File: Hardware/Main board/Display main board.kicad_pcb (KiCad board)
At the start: 2 copper layers, 142.2 x 91.4 mm, 55 parts, among them J1 Board to Board, J3 Conn_01x03, P1 USB_C_Plug_USB2.0, U1 BQ25895RTW, U10 W25Q32JVSS, U2 ABM8-272-T3, U4 RP2040, U5 AP7361C-33E, U6 AP7361C-33E, U7 AP7361C-33E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

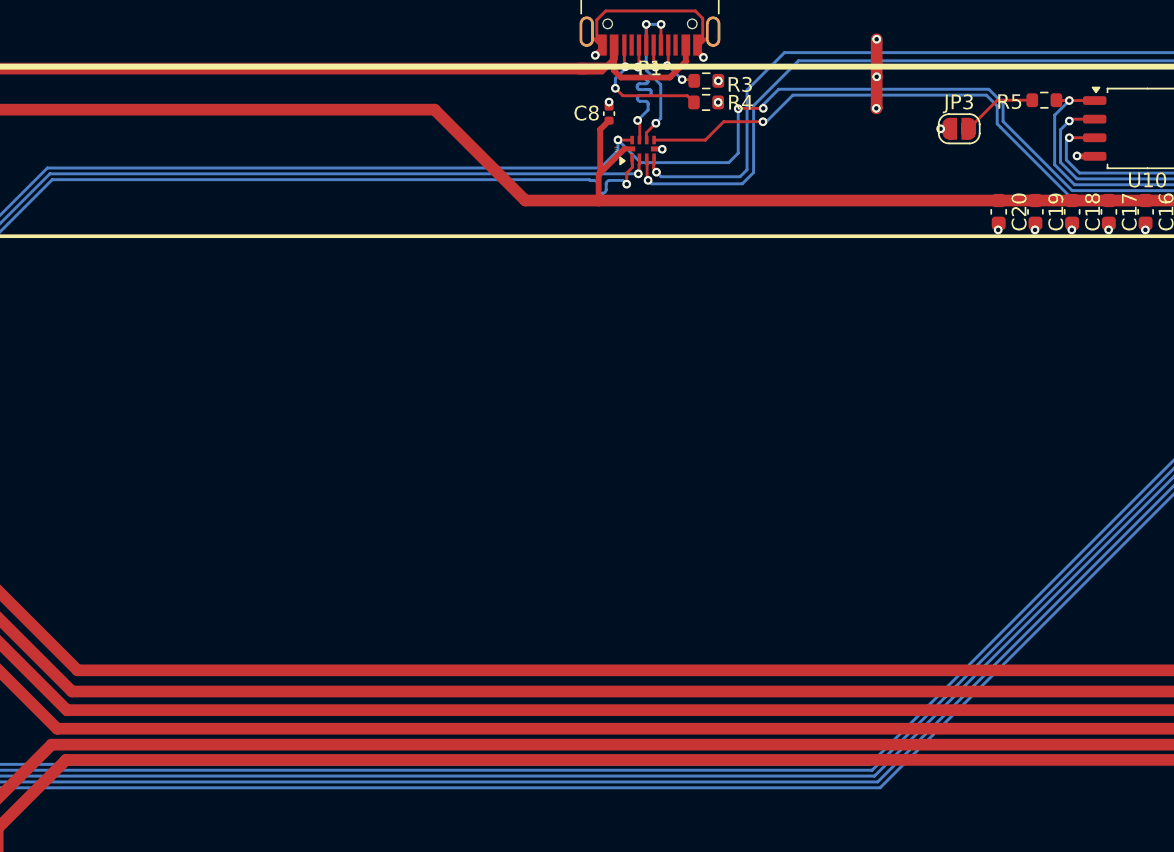
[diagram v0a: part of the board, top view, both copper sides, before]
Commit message: add battery label
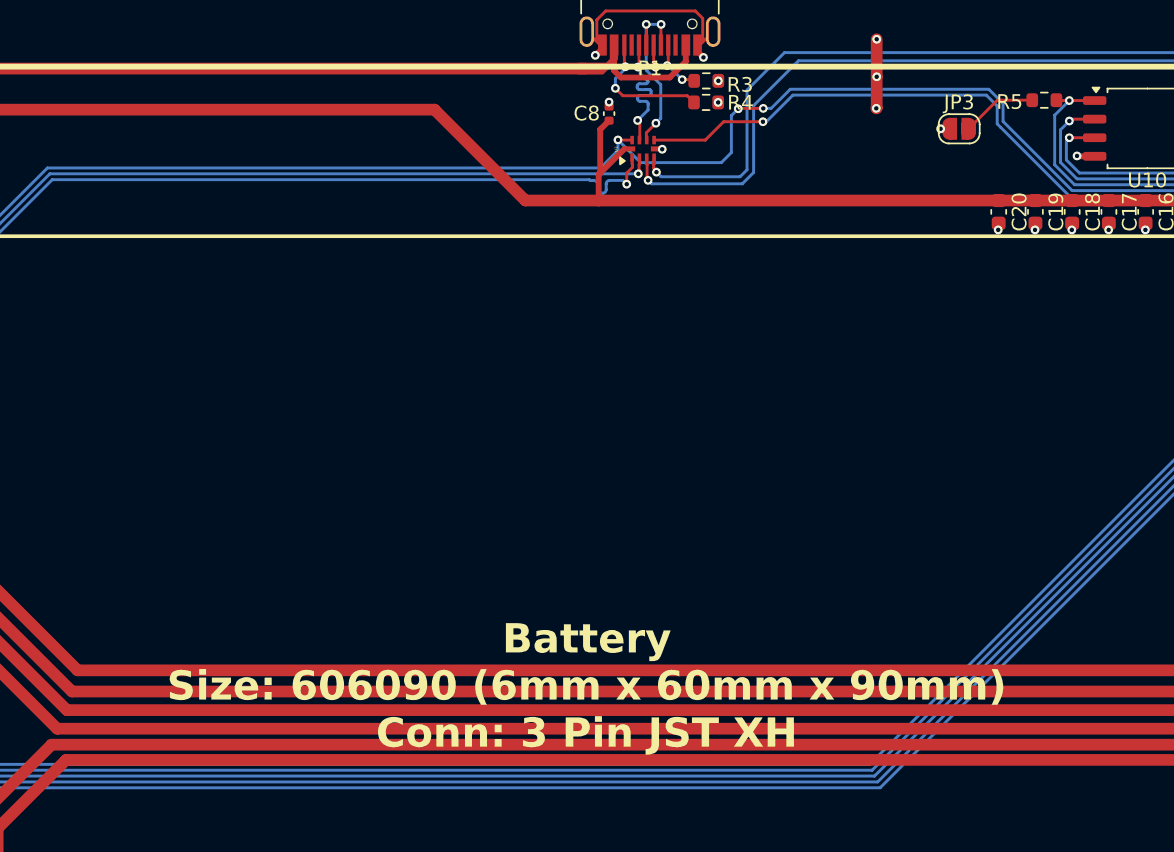
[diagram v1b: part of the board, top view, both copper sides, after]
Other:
- board text added: "Battery Size: 606090 (6mm x 60mm x 90mm) Conn: 3 Pin JST XH"
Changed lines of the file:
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@@
 		)
 	)
+	(gr_text "Battery\nSize: 606090 (6mm x 60mm x 90mm)\nConn: 3 Pin JST XH"
+		(at 132.842 107.1372 0)
+		(layer "F.SilkS")
+		(effects
+			(font
+				(size 2 2)
+				(thickness 0.4)
+				(bold yes)
+			)
+			(justify bottom)
+		)
+	)
 	(gr_text "+3V3-1\n+3V3-3\n+5V\nMB_SDA\nGND"
 		(at 193.569237 101.6 90)
@@
 	)
 	(segment
-		(start 179.658256 68.891)
-		(end 182.261 71.493744)
+		(start 133.771871 67.345329)
+		(end 134.9756 66.1416)
 		(width 0.2)
 		(layer "B.Cu")
@@
 	)
 	(segment
-		(start 182.261 71.493744)
-		(end 182.261 71.938475)
+		(start 85.766808 106.9024)
+		(end 88.83 106.9024)
 		(width 0.2)
 		(layer "B.Cu")
@@
 	)
 	(segment
-		(start 133.771871 67.345329)
-		(end 134.9756 66.1416)
+		(start 144.903032 63.273697)
+		(end 145.438103 63.273697)
 		(width 0.2)
 		(layer "B.Cu")
@@
 	)
 	(segment
-		(start 136.525 66.9798)
-		(end 134.9756 65.4304)
+		(start 89.545 106.1874)
+		(end 89.545 73.782114)
 		(width 0.2)
 		(layer "B.Cu")
@@
 	)
 	(segment
-		(start 183.880925 73.5584)
-		(end 190.614397 73.5584)
+		(start 145.438103 63.273697)
+		(end 146.7458 61.966)
 		(width 0.2)
 		(layer "B.Cu")
@@
 	)
 	(segment
-		(start 85.766808 106.9024)
-		(end 88.83 106.9024)
+		(start 85.566808 106.7024)
+		(end 85.766808 106.9024)
 		(width 0.2)
 		(layer "B.Cu")
@@
 	)
 	(segment
-		(start 89.545 106.1874)
-		(end 89.545 73.782114)
+		(start 166.013628 68.891)
+		(end 179.658256 68.891)
 		(width 0.2)
 		(layer "B.Cu")
@@
 	)
 	(segment
-		(start 85.566808 106.7024)
-		(end 85.766808 106.9024)
+		(start 179.658256 68.891)
+		(end 182.261 71.493744)
 		(width 0.2)
 		(layer "B.Cu")
@@
 	)
 	(segment
-		(start 160.3148 61.966)
-		(end 161.29 62.9412)
+		(start 146.7458 61.966)
+		(end 160.3148 61.966)
 		(width 0.2)
 		(layer "B.Cu")
@@
 	)
 	(segment
-		(start 143.193 66.3316)
-		(end 142.5448 66.9798)
+		(start 136.525 66.9798)
+		(end 134.9756 65.4304)
 		(width 0.2)
 		(layer "B.Cu")
@@
 	)
 	(segment
-		(start 143.193 63.2968)
-		(end 143.193 66.3316)
+		(start 183.880925 73.5584)
+		(end 190.614397 73.5584)
 		(width 0.2)
 		(layer "B.Cu")
@@
 	)
 	(segment
-		(start 144.903032 63.021368)
-		(end 145.9584 61.966)
+		(start 142.0368 66.9798)
+		(end 136.525 66.9798)
 		(width 0.2)
 		(layer "B.Cu")
@@
 	)
 	(segment
-		(start 190.614397 73.5584)
-		(end 190.846928 73.325869)
+		(start 182.261 71.938475)
+		(end 183.880925 73.5584)
+		(width 0.2)
+		(layer "B.Cu")
+		(net 21)
+	)
+	(segment
+		(start 142.7226 63.7672)
+		(end 142.7226 66.294)
 		(width 0.2)
 		(layer "B.Cu")
@@
 	)
 	(segment
-		(start 145.9584 61.966)
-		(end 160.3148 61.966)
+		(start 143.193 63.2968)
+		(end 142.7226 63.7672)
 		(width 0.2)
 		(layer "B.Cu")
@@
 	)
 	(segment
-		(start 161.29 62.9412)
-		(end 161.29 64.167372)
+		(start 182.261 71.493744)
+		(end 182.261 71.938475)
 		(width 0.2)
 		(layer "B.Cu")
@@
 	)
 	(segment
-		(start 142.5448 66.9798)
-		(end 136.525 66.9798)
+		(start 161.29 64.167372)
+		(end 166.013628 68.891)
 		(width 0.2)
 		(layer "B.Cu")
@@
 	)
 	(segment
-		(start 134.9756 66.1416)
-		(end 134.9756 65.4304)
+		(start 190.614397 73.5584)
+		(end 190.846928 73.325869)
 		(width 0.2)
 		(layer "B.Cu")
@@
 	)
 	(segment
-		(start 182.261 71.938475)
-		(end 183.880925 73.5584)
+		(start 134.9756 66.1416)
+		(end 134.9756 65.4304)
 		(width 0.2)
 		(layer "B.Cu")
@@
 	)
 	(segment
-		(start 161.29 64.167372)
-		(end 166.013628 68.891)
+		(start 160.3148 61.966)
+		(end 161.29 62.9412)
 		(width 0.2)
 		(layer "B.Cu")
@@
 	)
 	(segment
-		(start 166.013628 68.891)
-		(end 179.658256 68.891)
+		(start 142.7226 66.294)
+		(end 142.0368 66.9798)
 		(width 0.2)
 		(layer "B.Cu")
@@
 	)
 	(segment
-		(start 144.903032 63.273697)
-		(end 144.903032 63.021368)
+		(start 161.29 62.9412)
+		(end 161.29 64.167372)
 		(width 0.2)
 		(layer "B.Cu")

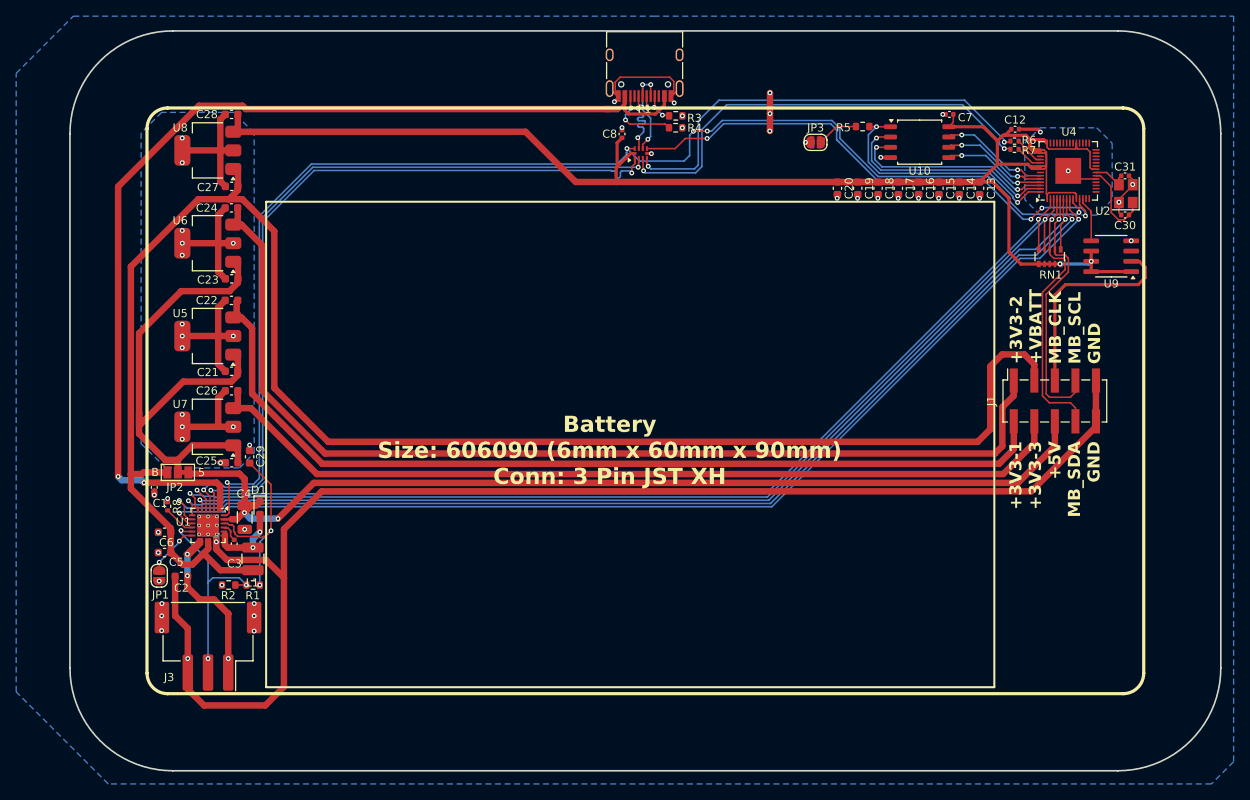
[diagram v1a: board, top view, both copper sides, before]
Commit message: Link USB-C port 3d model
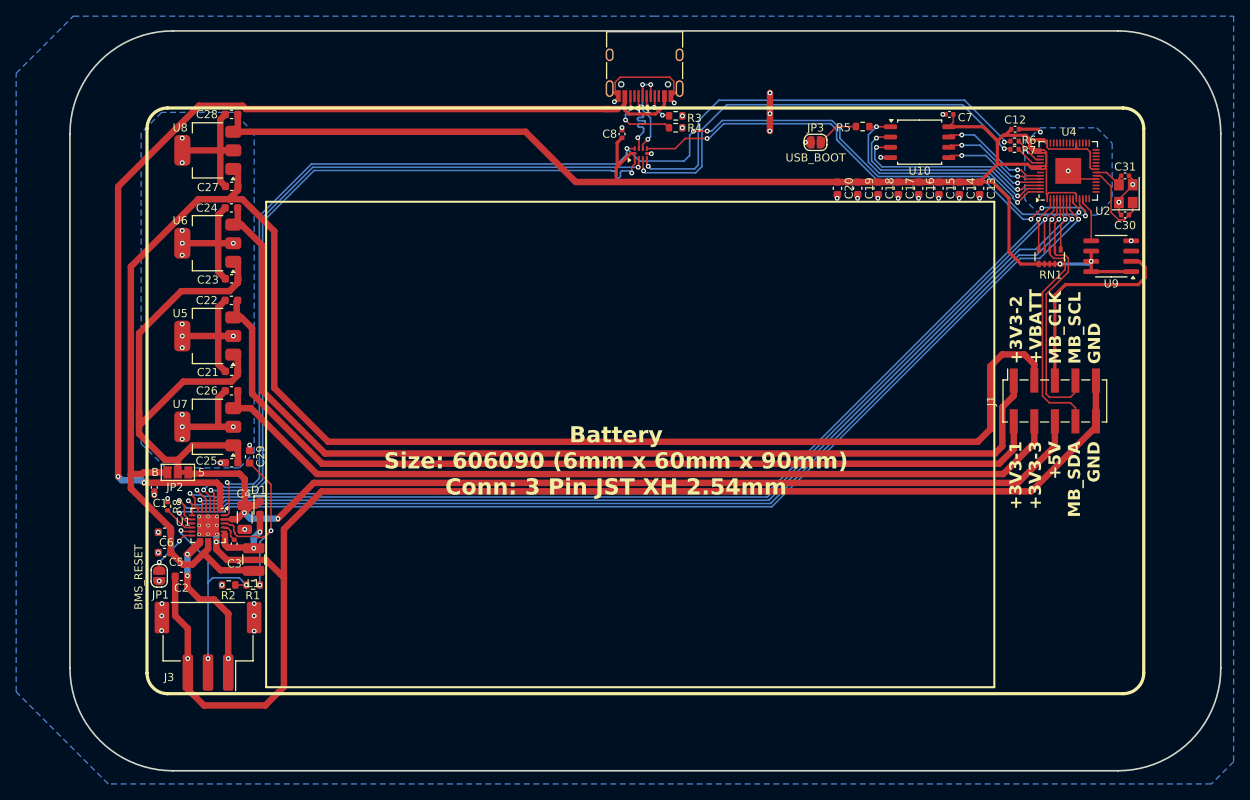
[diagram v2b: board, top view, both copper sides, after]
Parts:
- moved L1 0.13 mm to (88.8, 116.2)
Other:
- board text added: "Battery Size: 606090 (6mm x 60mm x 90mm) Conn: 3 Pin JST XH 2.54mm"
- board text removed: "Battery Size: 606090 (6mm x 60mm x 90mm) Conn: 3 Pin JST XH"
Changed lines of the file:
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@@
 		(property "Value" "USB_BOOT"
 			(at 0 1.9 0)
-			(layer "F.Fab")
+			(layer "F.SilkS")
 			(effects
 				(font
@@
 	(footprint "Inductor_SMD:L_1210_3225Metric"
 		(layer "F.Cu")
-		(at 88.7476 116.151201 -90)
+		(at 88.8492 116.2304 -90)
 		(descr "Inductor SMD 1210 (3225 Metric), square (rectangular) end terminal, IPC_7351 nominal, (Body size source: http://www.tortai-tech.com/upload/download/2011102023233369053.pdf), generated with kicad-footprint-generator")
 		(tags "inductor")
@@
 		)
 		(property "Value" "BMS_RESET"
-			(at -1.5136 -2.5908 90)
-			(layer "F.Fab")
+			(at -0.1778 -2.54 90)
+			(layer "F.SilkS")
 			(effects
 				(font
@@
 			)
 		)
+		(model "${KICAD8_3DMODEL_DIR}/Connector_USB.3dshapes/USB_C_Receptacle_GCT_USB4105-xx-A_16P_TopMnt_Horizontal.wrl"
+			(offset
+				(xyz 0 0 0)
+			)
+			(scale
+				(xyz 1 1 1)
+			)
+			(rotate
+				(xyz 0 0 0)
+			)
+		)
 	)
 	(footprint "Capacitor_SMD:C_0402_1005Metric"
@@
 		)
 	)
-	(gr_text "Battery\nSize: 606090 (6mm x 60mm x 90mm)\nConn: 3 Pin JST XH"
-		(at 132.842 107.1372 0)
+	(gr_text "Battery\nSize: 606090 (6mm x 60mm x 90mm)\nConn: 3 Pin JST XH 2.54mm"
+		(at 133.6294 108.4326 0)
 		(layer "F.SilkS")
 		(effects
@@
 	)
 	(segment
+		(start 84.7344 117.5512)
+		(end 82.6516 115.4684)
+		(width 0.8)
+		(layer "F.Cu")
+		(net 9)
+	)
+	(segment
+		(start 88.8492 117.630399)
+		(end 88.770001 117.5512)
+		(width 0.8)
+		(layer "F.Cu")
+		(net 9)
+	)
+	(segment
 		(start 78.6006 115.3668)
 		(end 78.6006 112.8568)
@@
 	)
 	(segment
-		(start 84.7344 117.5512)
-		(end 82.6516 115.4684)
-		(width 0.8)
-		(layer "F.Cu")
-		(net 9)
-	)
-	(segment
 		(start 91.3892 75.64424)
 		(end 91.3892 95.0214)
@@
 	)
 	(segment
-		(start 88.7476 117.5512)
-		(end 84.7344 117.5512)
-		(width 0.8)
-		(layer "F.Cu")
-		(net 9)
-	)
-	(segment
 		(start 179.8828 100.1268)
 		(end 179.8828 92.3544)
@@
 	)
 	(segment
+		(start 88.770001 117.5512)
+		(end 84.7344 117.5512)
+		(width 0.8)
+		(layer "F.Cu")
+		(net 9)
+	)
+	(segment
 		(start 87.44096 71.696)
 		(end 91.3892 75.64424)
@@
 	)
 	(segment
-		(start 85.287714 114.396114)
-		(end 85.287714 113.141186)
+		(start 85.642802 114.751202)
+		(end 85.287714 114.396114)
 		(width 0.8)
 		(layer "F.Cu")
@@
 	)
 	(segment
-		(start 85.642802 114.751202)
-		(end 85.287714 114.396114)
+		(start 88.8492 114.830401)
+		(end 88.770001 114.751202)
+		(width 0.8)
+		(layer "F.Cu")
+		(net 20)
+	)
+	(segment
+		(start 88.770001 114.751202)
+		(end 85.642802 114.751202)
 		(width 0.8)
 		(layer "F.Cu")
@@
 	)
 	(segment
-		(start 88.7476 114.751202)
-		(end 85.642802 114.751202)
+		(start 85.287714 114.396114)
+		(end 85.287714 113.141186)
 		(width 0.8)
 		(layer "F.Cu")
@@
 	)
 	(via
-		(at 88.7476 114.751202)
+		(at 88.8492 114.830401)
 		(size 0.6)
 		(drill 0.3)
@@
 	)
 	(segment
-		(start 88.7476 113.6904)
+		(start 88.8492 113.5888)
 		(end 89.6112 112.8268)
 		(width 0.8)
@@
 	)
 	(segment
-		(start 88.7476 114.751202)
-		(end 88.7476 113.6904)
+		(start 88.8492 114.830401)
+		(end 88.8492 113.5888)
 		(width 0.8)
 		(layer "B.Cu")

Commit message: Change board size + mounting holes
still need to finish re-routing the front plate
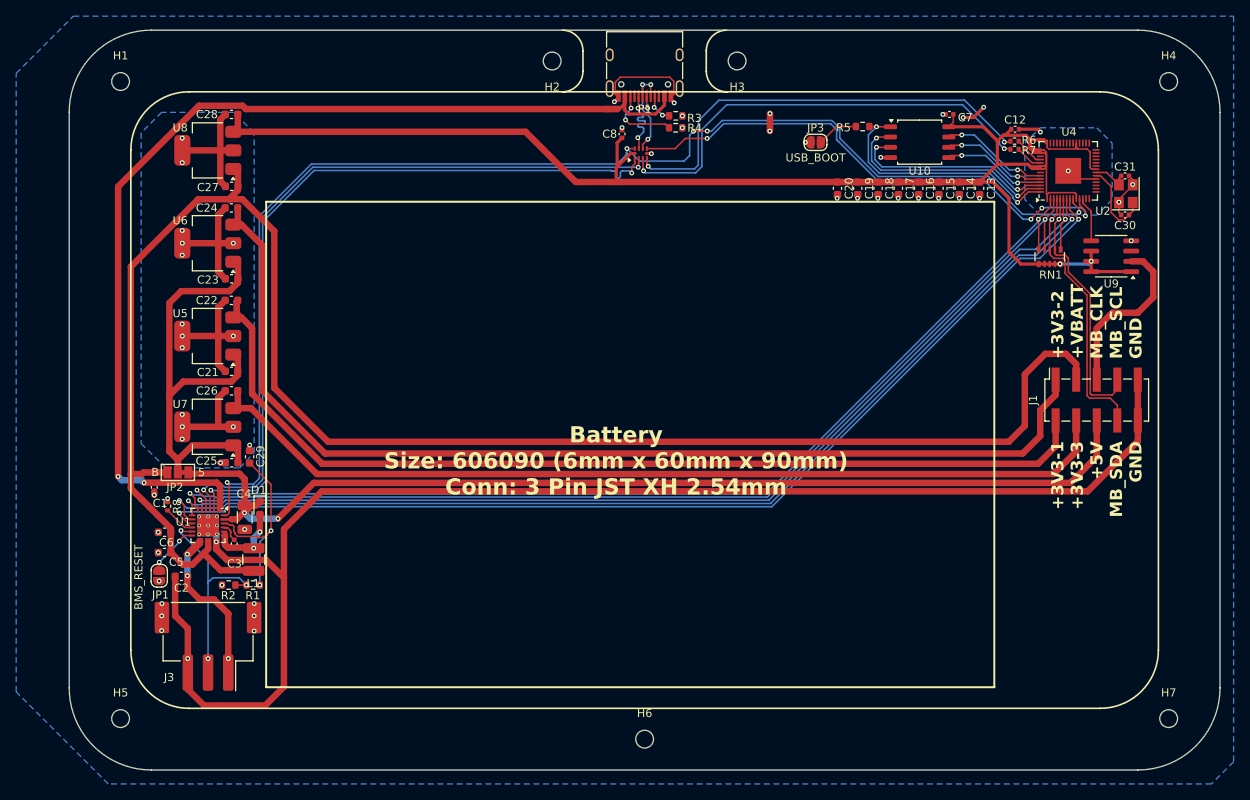
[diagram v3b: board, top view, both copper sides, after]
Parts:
- added H1: MountingHole, MountingHole:MountingHole_2.2mm_M2, F.Cu at (72.4, 57.1)
- added H2: MountingHole, MountingHole:MountingHole_2.2mm_M2, F.Cu at (125.7, 54.6)
- added H3: MountingHole, MountingHole:MountingHole_2.2mm_M2, F.Cu at (148.6, 54.6)
- added H4: MountingHole, MountingHole:MountingHole_2.2mm_M2, F.Cu at (201.9, 57.1)
- added H5: MountingHole, MountingHole:MountingHole_2.2mm_M2, F.Cu at (72.4, 135.9)
- added H6: MountingHole, MountingHole:MountingHole_2.2mm_M2, F.Cu at (137.2, 138.4)
- added H7: MountingHole, MountingHole:MountingHole_2.2mm_M2, F.Cu at (201.9, 135.9)
- moved J1 5.18 mm to (193.0, 96.5)
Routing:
- net /Power managment/VIN: track 66.9 -> 55.9 mm
- net GND: track 268.8 -> 275.6 mm, vias 50 -> 51
- net +5V: track 124.4 -> 130.5 mm
- net +3v3-3: track 109.5 -> 115.4 mm
- net +3v3-1: track 115.2 -> 120.3 mm
- net MB_CLK: track 25.9 -> 21.4 mm
- net +VBATT: track 210.9 -> 215.2 mm
- net +3v3-2: track 128.6 -> 132.9 mm
- net MB_SCL: track 32.3 -> 31.7 mm
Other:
- outline, holes or cut-outs redrawn
